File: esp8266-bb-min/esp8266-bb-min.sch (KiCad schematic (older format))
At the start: 15 parts, among them J1 Conn_01x02_Male, J2 Conn_02x08_Odd_Even, U1 LP38693MP-3.3, U2 ESP-12F

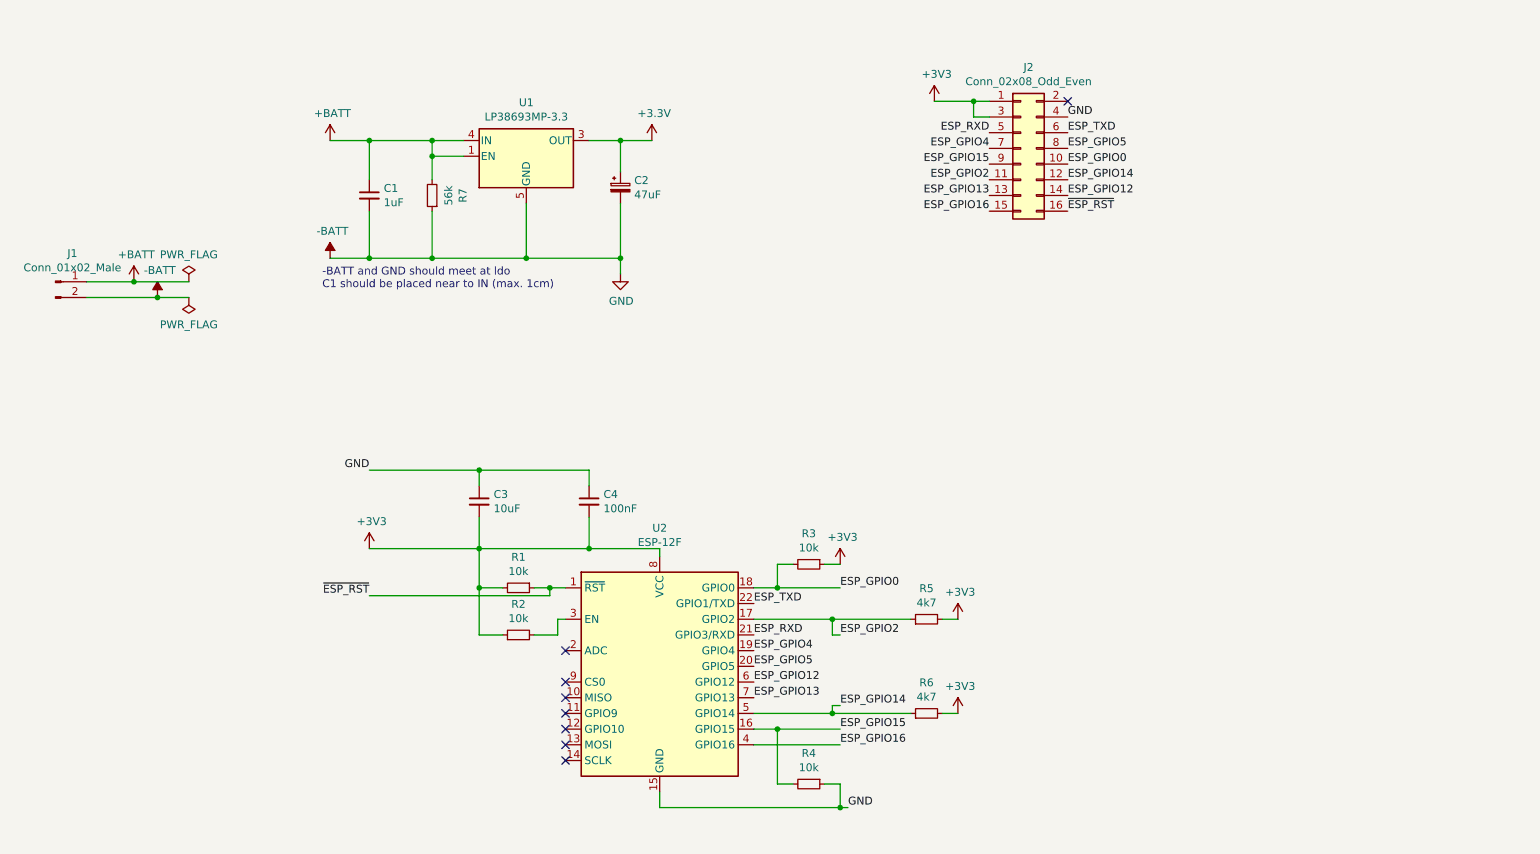
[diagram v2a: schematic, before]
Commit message: sch: addressed issue domi3006/esp8266-bb-min#4
Signed-off-by: Dominik Laton <dominik.laton@web.de>
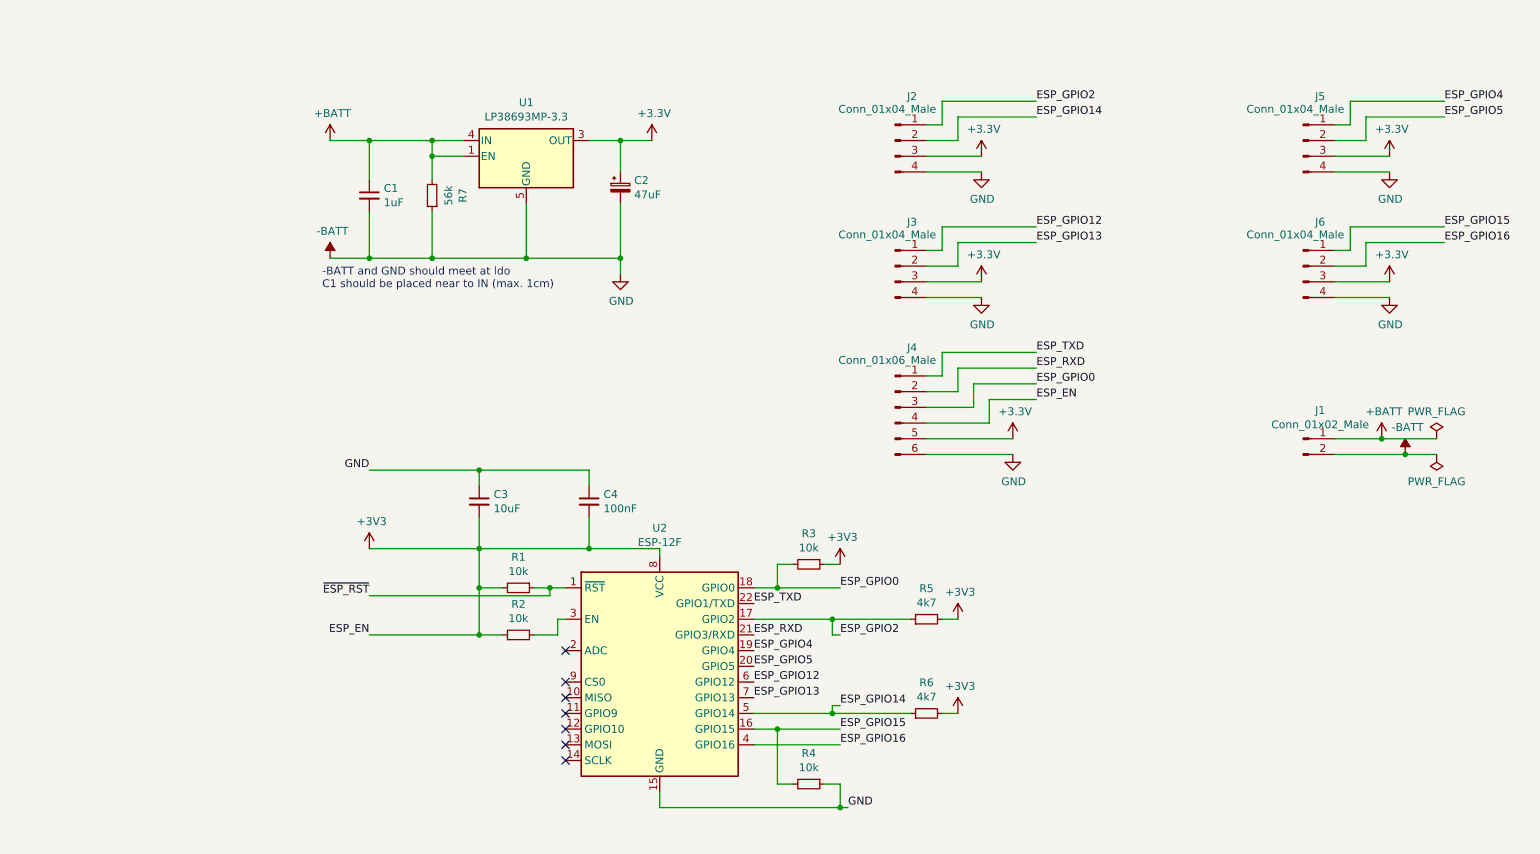
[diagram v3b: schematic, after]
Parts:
- removed J2: Conn_02x08_Odd_Even, Connector_PinHeader_2.54mm:PinHeader_2x08_P2.54mm_Vertical_SMD, symbol Connector_Generic:Conn_02x08_Odd_Even
- added J2, J3, J5, J6: Conn_01x04_Male, Connector_JST:JST_XH_B4B-XH-A_1x04_P2.50mm_Vertical, symbol Connector:Conn_01x04_Male
- added J4: Conn_01x06_Male, Connector_JST:JST_XH_B6B-XH-A_1x06_P2.50mm_Vertical, symbol Connector:Conn_01x06_Male
- J1: footprint Connector_PinHeader_2.54mm:PinHeader_1x02_P2.54mm_Horizontal -> Connector_JST:JST_XH_B2B-XH-A_1x02_P2.50mm_Vertical
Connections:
- net +3V3: now also J2.3 (Pin_3), J3.3 (Pin_3), J4.4 (Pin_4), J4.5 (Pin_5), J5.3 (Pin_3), J6.3 (Pin_3)
- net -BATT: now also J2.4 (Pin_4), J3.4 (Pin_4), J4.6 (Pin_6), J5.4 (Pin_4), J6.4 (Pin_4)
- net ESP_GPIO0: now also J4.3 (Pin_3)
- net ESP_GPIO12: now also J3.1 (Pin_1)
- net ESP_GPIO13: now also J3.2 (Pin_2)
- net ESP_GPIO14: now also J2.2 (Pin_2)
- net ESP_GPIO15: now also J6.1 (Pin_1)
- net ESP_GPIO16: now also J6.2 (Pin_2)
- net ESP_GPIO2: now also J2.1 (Pin_1)
- net ESP_GPIO4: now also J5.1 (Pin_1)
- net ESP_GPIO5: now also J5.2 (Pin_2)
- net ESP_RXD: now also J4.2 (Pin_2)
- net ESP_TXD: now also J4.1 (Pin_1)
- no-connect marks 8 -> 7
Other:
- moved on the sheet: J1

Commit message: sch: addressed issue domi3006/esp8266-bb-min#5
Signed-off-by: Dominik Laton <dominik.laton@web.de>
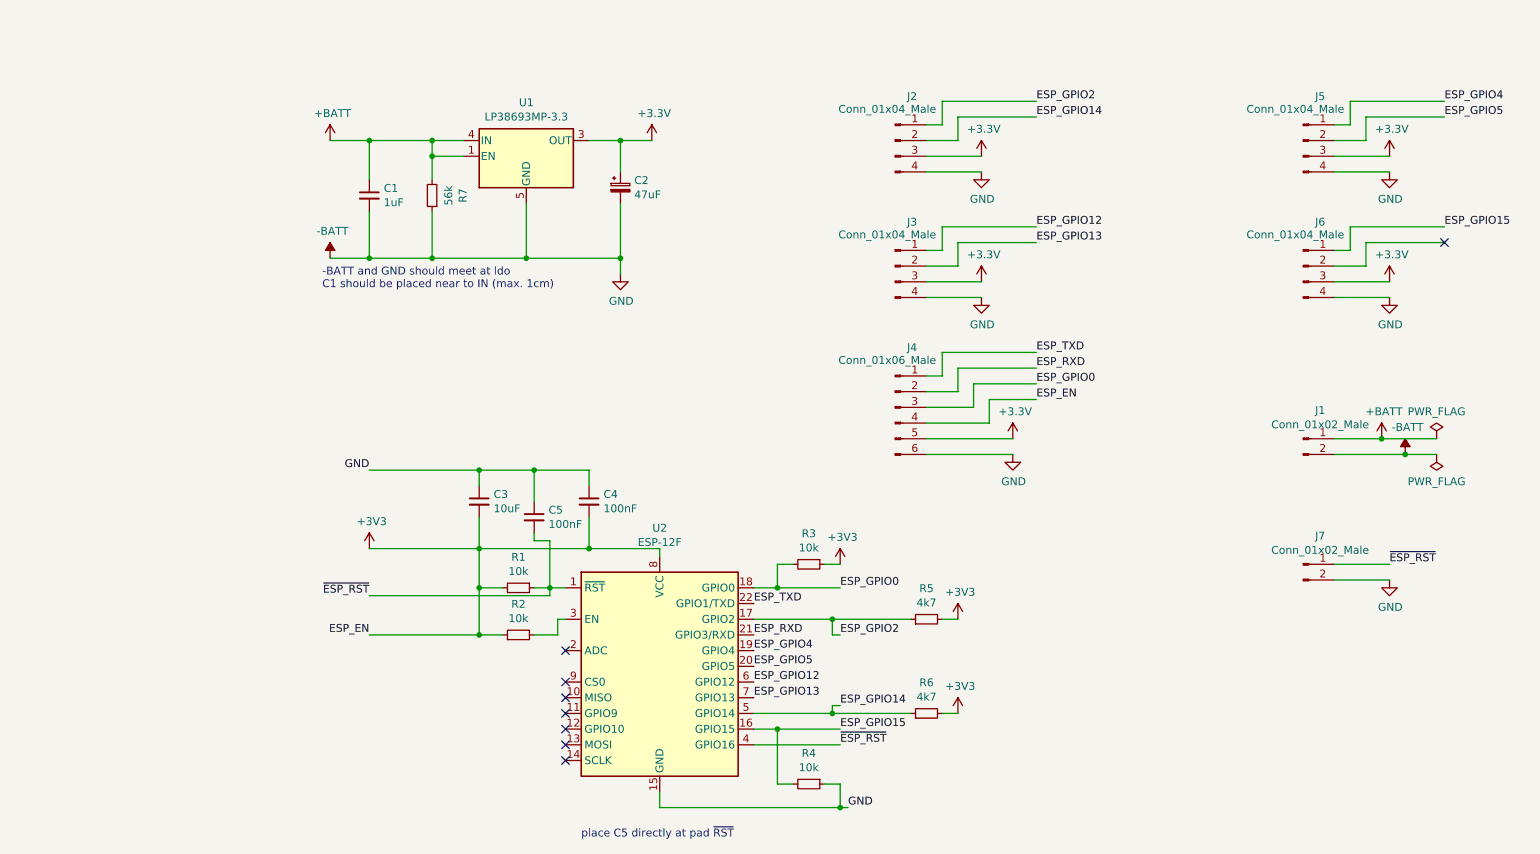
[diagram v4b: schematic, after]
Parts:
- added C5: 100nF, Capacitor_SMD:C_0805_2012Metric_Pad1.18x1.45mm_HandSolder, symbol Device:C_Small
- added J7: Conn_01x02_Male, Connector_JST:JST_XH_B2B-XH-A_1x02_P2.50mm_Vertical, symbol Connector:Conn_01x02_Male
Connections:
- net -BATT: now also C5.1, J7.2 (Pin_2)
- net ~ESP_RST: now also U2.4 (GPIO16), C5.2, J7.1 (Pin_1)
- net ESP_GPIO16: no longer names the net of J6.2 (Pin_2)
- net ESP_GPIO16: no longer U2.4 (GPIO16)
- no-connect marks 7 -> 8
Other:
- note added: "place C5 directly at pad ~RST"
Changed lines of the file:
@@
 	4400 3600 4400 3500
 Wire Wire Line
-	4400 3500 3700 3500
+	4400 3500 4050 3500
 Wire Wire Line
 	3700 3600 3700 3500
@@
 	6000 5650 6050 5650
 Text Label 6000 5250 0    50   ~ 0
-ESP_GPIO16
+~ESP_RST
 Text Label 6000 5150 0    50   ~ 0
 ESP_GPIO15
@@
 Wire Wire Line
 	9350 2200 9350 2050
-Wire Wire Line
-	9350 2050 9850 2050
 Wire Wire Line
 	9150 2100 9250 2100
@@
 Text Label 9850 1950 0    50   ~ 0
 ESP_GPIO15
-Text Label 9850 2050 0    50   ~ 0
-ESP_GPIO16
 $Comp
 L Connector:Conn_01x06_Male J4
@@
 Text Label 3000 4550 2    50   ~ 0
 ESP_EN
+$Comp
+L Device:C_Small C5
+U 1 1 5FC2756C
+P 4050 3800
+F 0 "C5" H 4142 3846 50  0000 L CNN
+F 1 "100nF" H 4142 3755 50  0000 L CNN
+F 2 "Capacitor_SMD:C_0805_2012Metric_Pad1.18x1.45mm_HandSolder" H 4050 3800 50  0001 C CNN
+F 3 "~" H 4050 3800 50  0001 C CNN
+	1    4050 3800
+	1    0    0    -1
+$EndComp
+Wire Wire Line
+	4150 4250 4150 3950
+Wire Wire Line
+	4150 3950 4050 3950
+Wire Wire Line
+	4050 3950 4050 3900
+Wire Wire Line
+	4050 3700 4050 3500
+Connection ~ 4050 3500
+Wire Wire Line
+	4050 3500 3700 3500
+Text Notes 4350 5850 0    50   ~ 0
+place C5 directly at pad ~RST
+$Comp
+L Connector:Conn_01x02_Male J7
+U 1 1 5FC27C22
+P 8950 4100
+F 0 "J7" H 9058 4281 50  0000 C CNN
+F 1 "Conn_01x02_Male" H 9058 4190 50  0000 C CNN
+F 2 "Connector_JST:JST_XH_B2B-XH-A_1x02_P2.50mm_Vertical" H 8950 4100 50  0001 C CNN
+F 3 "~" H 8950 4100 50  0001 C CNN
+	1    8950 4100
+	1    0    0    -1
+$EndComp
+Wire Wire Line
+	9150 4200 9500 4200
+Wire Wire Line
+	9150 4100 9500 4100
+Text Label 9500 4100 0    50   ~ 0
+~ESP_RST
+$Comp
+L power:GND #PWR011
+U 1 1 5FC3B1D1
+P 9500 4200
+F 0 "#PWR011" H 9500 3950 50  0001 C CNN
+F 1 "GND" H 9505 4027 50  0000 C CNN
+F 2 "" H 9500 4200 50  0001 C CNN
+F 3 "" H 9500 4200 50  0001 C CNN
+	1    9500 4200
+	1    0    0    -1
+$EndComp
+Wire Wire Line
+	9350 2050 9850 2050
+NoConn ~ 9850 2050
 $EndSCHEMATC

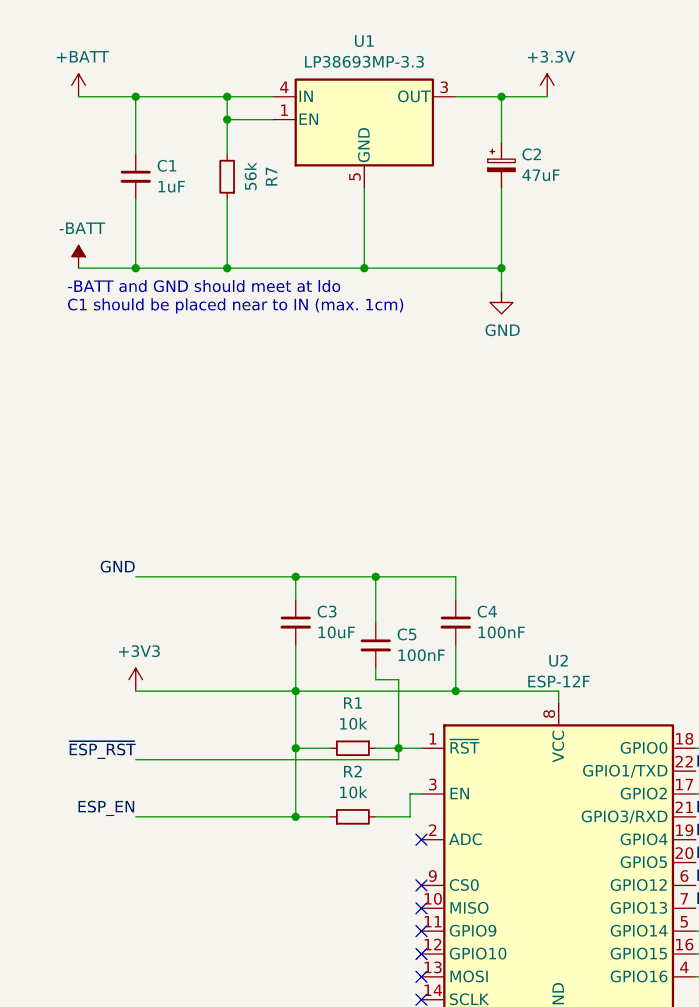
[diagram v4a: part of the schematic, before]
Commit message: sch: added adc sensing for battery
Signed-off-by: Dominik Laton <dominik.laton@web.de>
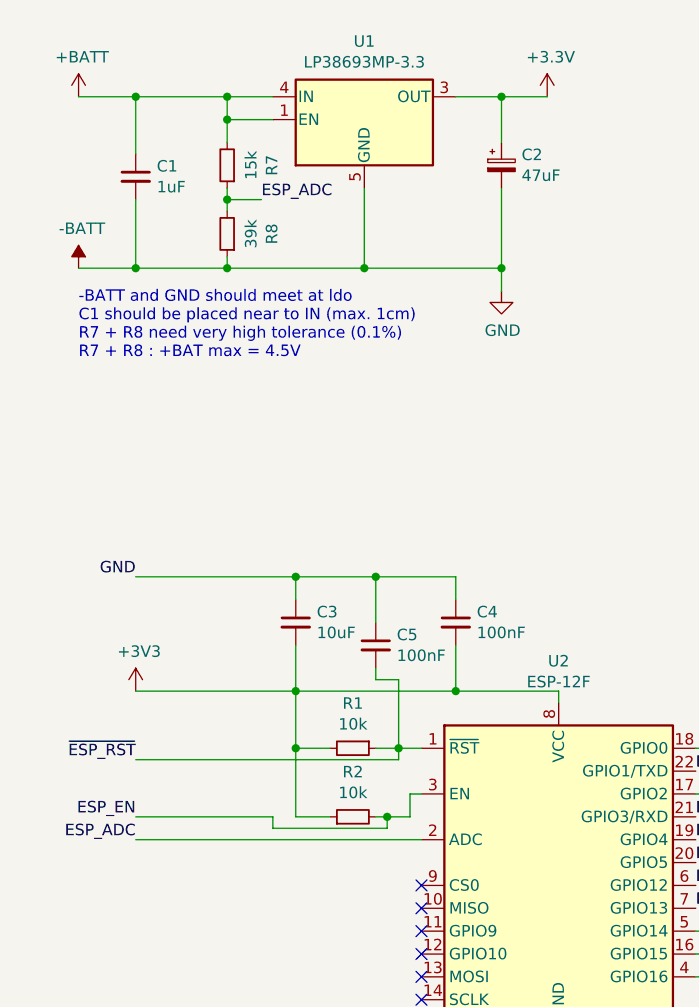
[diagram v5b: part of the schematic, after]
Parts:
- added R8: 39k, Resistor_SMD:R_0805_2012Metric_Pad1.20x1.40mm_HandSolder, symbol Device:R_Small
- R7: value 56k -> 15k
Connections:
- net +3V3: no longer J4.4 (Pin_4)
- net -BATT: now also R8.1; no longer R7.1
- net ESP_ADC: now reaches U2.2 (ADC)
- net ESP_ADC: now also R7.1, R8.2
- net ESP_EN: now reaches R2.2, U2.3 (EN)
- net ESP_EN: now also J4.4 (Pin_4)
- no-connect marks 8 -> 7
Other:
- note added: "-BATT and GND should meet at ldo\nC1 should be placed near to IN (max. 1cm)\nR7 + R8 need very high tolerance (0.1%)\nR7 + R8 : +BAT max = 4.5V"
- note removed: "-BATT and GND should meet at ldo\nC1 should be placed near to IN (max. 1cm)"
- moved on the sheet: R7
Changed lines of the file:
@@
-	1    0    0    -1
-$EndComp
-$Comp
-L Device:CP_Small C2
-U 1 1 5FA30A7D
-P 4600 1700
-F 0 "C2" H 4688 1746 50  0000 L CNN
-F 1 "47uF" H 4688 1655 50  0000 L CNN
-F 2 "Capacitor_SMD:CP_Elec_6.3x9.9" H 4600 1700 50  0001 C CNN
-F 3 "~" H 4600 1700 50  0001 C CNN
-	1    4600 1700
 	1    0    0    -1
 $EndComp
@@
 	4200 4450 4200 4550
 Wire Wire Line
-	4200 4550 4050 4550
+	4200 4550 4100 4550
 Wire Wire Line
 	3850 4550 3700 4550
@@
 	3700 4550 3700 4250
 Connection ~ 3700 4250
-NoConn ~ 4250 4650
 $Comp
 L Device:R_Small R3
@@
 	3000 1400 3000 1650
 Wire Wire Line
-	3000 2150 3400 2150
-Wire Wire Line
 	4000 1800 4000 2150
 Connection ~ 4000 2150
@@
 L Device:R_Small R7
 U 1 1 5FC4664C
-P 3400 1750
-F 0 "R7" V 3204 1750 50  0000 C CNN
-F 1 "56k" V 3295 1750 50  0000 C CNN
-F 2 "Resistor_SMD:R_0805_2012Metric_Pad1.20x1.40mm_HandSolder" H 3400 1750 50  0001 C CNN
-F 3 "~" H 3400 1750 50  0001 C CNN
-	1    3400 1750
+P 3400 1700
+F 0 "R7" V 3204 1700 50  0000 C CNN
+F 1 "15k" V 3295 1700 50  0000 C CNN
+F 2 "Resistor_SMD:R_0805_2012Metric_Pad1.20x1.40mm_HandSolder" H 3400 1700 50  0001 C CNN
+F 3 "~" H 3400 1700 50  0001 C CNN
+	1    3400 1700
 	-1   0    0    1
 $EndComp
@@
 Wire Wire Line
 	3400 1400 3000 1400
-Wire Wire Line
-	3400 1500 3400 1650
-Connection ~ 3400 1500
-Wire Wire Line
-	3400 1850 3400 2150
-Connection ~ 3400 2150
-Wire Wire Line
-	3400 2150 4000 2150
 $Comp
 L power:+3.3V #PWR0110
@@
 Wire Wire Line
 	9600 3400 9800 3400
-Text Notes 2700 2350 0    50   ~ 0
--BATT and GND should meet at ldo\nC1 should be placed near to IN (max. 1cm)
+Text Notes 2750 2550 0    50   ~ 0
+-BATT and GND should meet at ldo\nC1 should be placed near to IN (max. 1cm)\nR7 + R8 need very high tolerance (0.1%)\nR7 + R8 : +BAT max = 4.5V
 $Comp
 L Connector:Conn_01x04_Male J2
@@
 Text Label 7250 3050 0    50   ~ 0
 ESP_EN
-Wire Wire Line
-	3700 4550 3000 4550
-Connection ~ 3700 4550
 Text Label 3000 4550 2    50   ~ 0
 ESP_EN
@@
 	9350 2050 9850 2050
 NoConn ~ 9850 2050
+$Comp
+L Device:R_Small R8
+U 1 1 5FC28F9A
+P 3400 2000
+F 0 "R8" V 3204 2000 50  0000 C CNN
+F 1 "39k" V 3295 2000 50  0000 C CNN
+F 2 "Resistor_SMD:R_0805_2012Metric_Pad1.20x1.40mm_HandSolder" H 3400 2000 50  0001 C CNN
+F 3 "~" H 3400 2000 50  0001 C CNN
+	1    3400 2000
+	-1   0    0    1
+$EndComp
+Wire Wire Line
+	3000 2150 3400 2150
+Wire Wire Line
+	3400 1500 3400 1600
+Connection ~ 3400 1500
+Wire Wire Line
+	3400 1800 3400 1850
+Wire Wire Line
+	3400 2100 3400 2150
+Connection ~ 3400 2150
+Wire Wire Line
+	3400 2150 4000 2150
+Wire Wire Line
+	3400 1850 3550 1850
+Connection ~ 3400 1850
+Wire Wire Line
+	3400 1850 3400 1900
+Text Label 3550 1850 0    50   ~ 0
+ESP_ADC
+Text Label 3000 4650 2    50   ~ 0
+ESP_ADC
+$Comp
+L Device:CP_Small C2
+U 1 1 5FA30A7D
+P 4600 1700
+F 0 "C2" H 4688 1746 50  0000 L CNN
+F 1 "47uF" H 4688 1655 50  0000 L CNN
+F 2 "Capacitor_SMD:CP_Elec_6.3x9.9" H 4600 1700 50  0001 C CNN
+F 3 "~" H 4600 1700 50  0001 C CNN
+	1    4600 1700
+	1    0    0    -1
+$EndComp
+Wire Wire Line
+	3000 4550 3600 4550
+Wire Wire Line
+	3600 4550 3600 4600
+Wire Wire Line
+	3600 4600 4100 4600
+Wire Wire Line
+	4100 4600 4100 4550
+Connection ~ 4100 4550
+Wire Wire Line
+	4100 4550 4050 4550
+Wire Wire Line
+	3000 4650 4250 4650
 $EndSCHEMATC

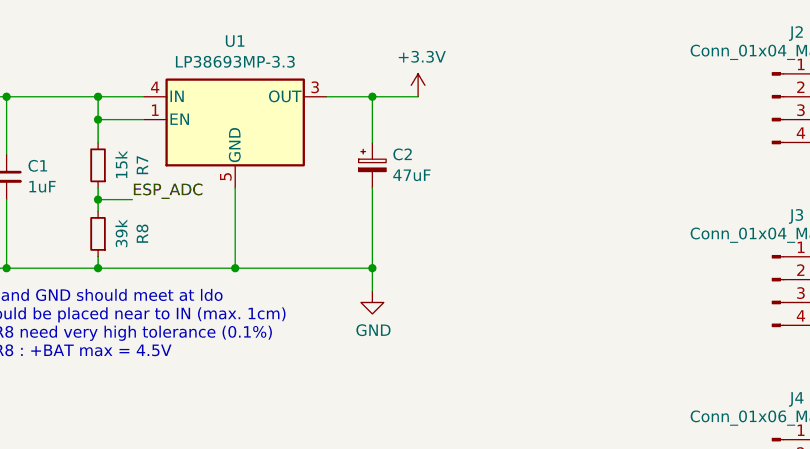
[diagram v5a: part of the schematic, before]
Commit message: sch: used ceramic condensator X5R for C2
Signed-off-by: Dominik Laton <dominik.laton@web.de>
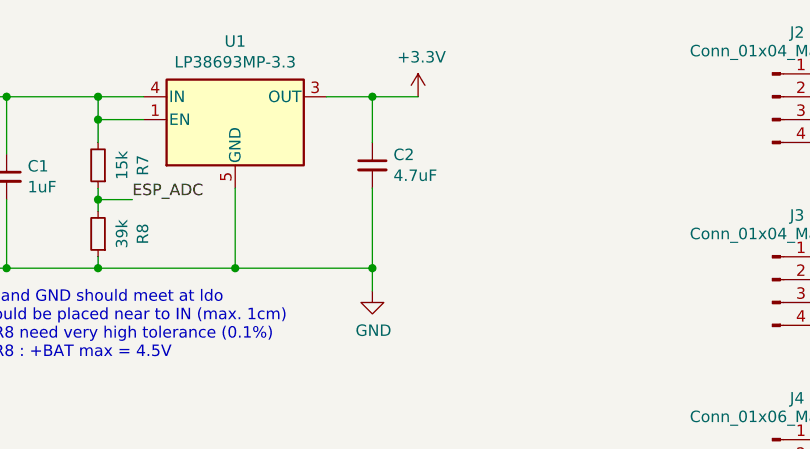
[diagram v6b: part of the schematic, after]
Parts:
- removed C2: 47uF, Capacitor_SMD:CP_Elec_6.3x9.9, symbol Device:CP_Small
- added C2: 4.7uF, Capacitor_SMD:C_0805_2012Metric_Pad1.18x1.45mm_HandSolder, symbol Device:C_Small
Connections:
- net +3V3: now also C2.1
- net -BATT: now also C2.2
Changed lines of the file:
@@
 ESP_ADC
 $Comp
-L Device:CP_Small C2
-U 1 1 5FA30A7D
+L Device:C_Small C2
+U 1 1 5FC52789
 P 4600 1700
-F 0 "C2" H 4688 1746 50  0000 L CNN
-F 1 "47uF" H 4688 1655 50  0000 L CNN
-F 2 "Capacitor_SMD:CP_Elec_6.3x9.9" H 4600 1700 50  0001 C CNN
+F 0 "C2" H 4692 1746 50  0000 L CNN
+F 1 "4.7uF" H 4692 1655 50  0000 L CNN
+F 2 "Capacitor_SMD:C_0805_2012Metric_Pad1.18x1.45mm_HandSolder" H 4600 1700 50  0001 C CNN
 F 3 "~" H 4600 1700 50  0001 C CNN
 	1    4600 1700
